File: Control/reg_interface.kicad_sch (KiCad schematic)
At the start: 16 parts, among them J5 Conn_01x04, J6 Conn_01x04, J7 Conn_01x02, J8 Conn_01x04, U10 74AHC1G08, U11 74AHC1G04, U12 74AHC1G32, U13 74AHC1G00, U14 74AHC1G32, U15 74HC173

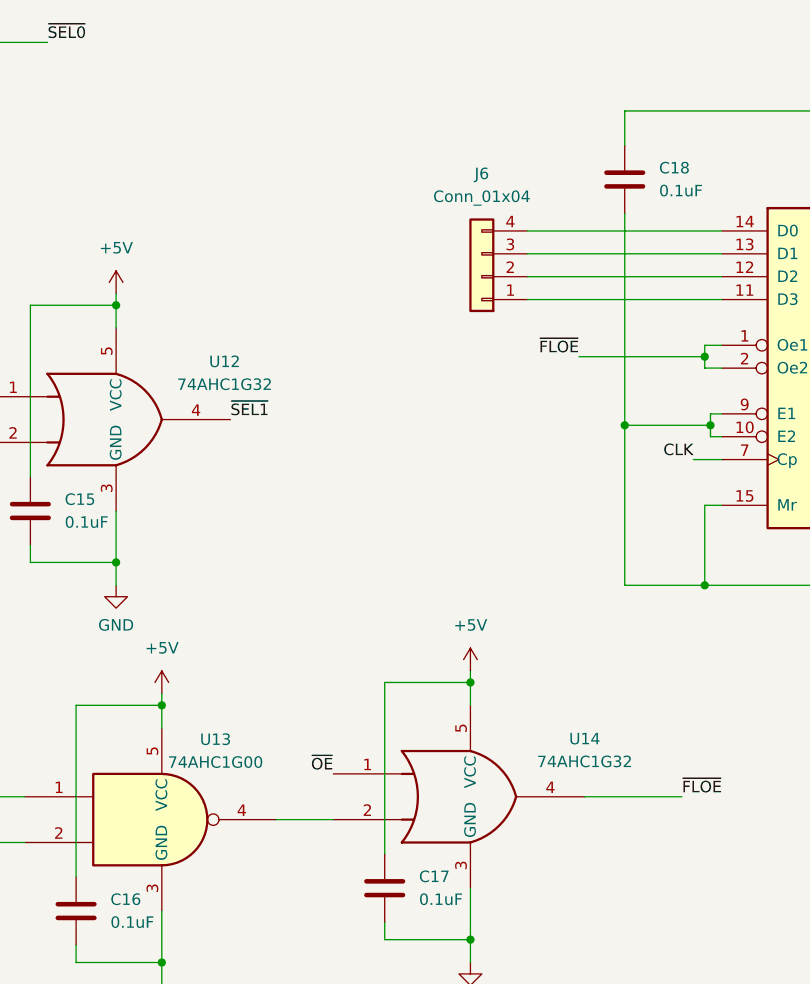
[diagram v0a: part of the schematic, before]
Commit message: Cleanup, added photos and README overhaul
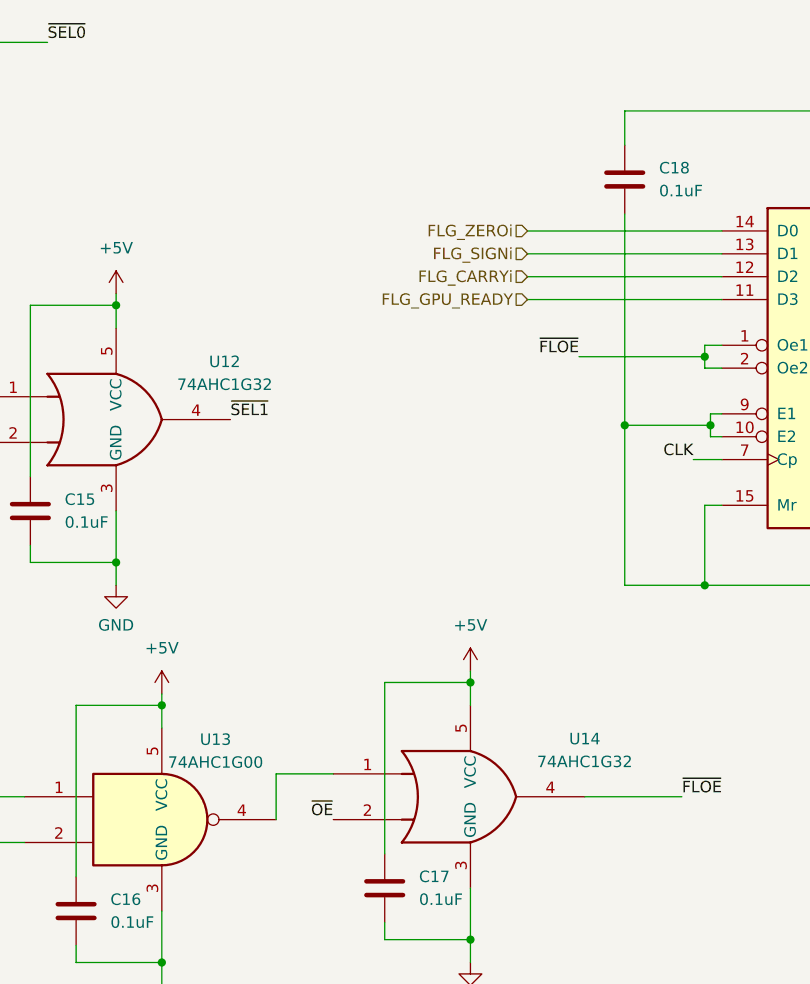
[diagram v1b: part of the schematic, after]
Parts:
- removed J6: Conn_01x04, Connector_PinSocket_2.54mm:PinSocket_1x04_P2.54mm_Vertical, symbol Connector_Generic:Conn_01x04
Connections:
- net ~{OE}: now also U14.2; no longer U14.1
- net at U13.4: now also U14.1; no longer U14.2
- net FLG_GPU_READY: now reaches U15.11 (D3)
- net FLG_CARRYi: now reaches U15.12 (D2)
- net FLG_SIGNi: now reaches U15.13 (D1)
- net FLG_ZEROi: now reaches U15.14 (D0)
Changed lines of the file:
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@@
+	(wire
+		(pts
+			(xy 111.125 109.22) (xy 111.125 104.14)
+		)
+		(stroke
+			(width 0)
+			(type default)
+		)
+	)
 	(wire
 		(pts
@@
 	(wire
 		(pts
-			(xy 111.125 109.22) (xy 117.475 109.22)
-		)
-		(stroke
-			(width 0)
-			(type default)
-		)
-	)
-	(wire
-		(pts
 			(xy 98.425 119.38) (xy 98.425 125.095)
 		)
@@
 		(pts
 			(xy 64.135 80.645) (xy 78.105 80.645)
+		)
+		(stroke
+			(width 0)
+			(type default)
+		)
+	)
+	(wire
+		(pts
+			(xy 111.125 104.14) (xy 117.475 104.14)
 		)
 		(stroke
@@
 		)
 	)
+	(label "~{OE}"
+		(at 117.475 109.22 180)
+		(effects
+			(font
+				(size 1.27 1.27)
+			)
+			(justify right bottom)
+		)
+	)
 	(label "R1"
 		(at 26.035 28.575 0)
@@
 		)
 	)
-	(label "~{OE}"
-		(at 117.475 104.14 180)
-		(effects
-			(font
-				(size 1.27 1.27)
-			)
-			(justify right bottom)
-		)
-	)
 	(label "R2"
 		(at 73.025 22.86 180)
@@
 			)
 			(justify right bottom)
+		)
+	)
+	(hierarchical_label "FLG_GPU_READY"
+		(shape input)
+		(at 139.065 51.435 180)
+		(effects
+			(font
+				(size 1.27 1.27)
+			)
+			(justify right)
+		)
+	)
+	(hierarchical_label "FLG_SIGNi"
+		(shape input)
+		(at 139.065 46.355 180)
+		(effects
+			(font
+				(size 1.27 1.27)
+			)
+			(justify right)
+		)
+	)
+	(hierarchical_label "FLG_ZEROi"
+		(shape input)
+		(at 139.065 43.815 180)
+		(effects
+			(font
+				(size 1.27 1.27)
+			)
+			(justify right)
+		)
+	)
+	(hierarchical_label "FLG_CARRYi"
+		(shape input)
+		(at 139.065 48.895 180)
+		(effects
+			(font
+				(size 1.27 1.27)
+			)
+			(justify right)
 		)
 	)
@@
 	)
 	(symbol
+		(lib_id "Device:C")
+		(at 37.465 55.88 0)
+		(unit 1)
+		(exclude_from_sim no)
+		(in_bom yes)
+		(on_board yes)
+		(dnp no)
+		(fields_autoplaced yes)
+		(property "Reference" "C13"
+			(at 40.64 54.6099 0)
+			(effects
+				(font
+					(size 1.27 1.27)
+				)
+				(justify left)
+			)
+		)
+		(property "Value" "0.1uF"
+			(at 40.64 57.1499 0)
+			(effects
+				(font
+					(size 1.27 1.27)
+				)
+				(justify left)
+			)
+		)
+		(property "Footprint" "Capacitor_SMD:C_0603_1608Metric"
+			(at 38.4302 59.69 0)
+			(effects
+				(font
+					(size 1.27 1.27)
+				)
+				(hide yes)
+			)
+		)
+		(property "Datasheet" "~"
+			(at 37.465 55.88 0)
+			(effects
+				(font
+					(size 1.27 1.27)
+				)
+				(hide yes)
+			)
+		)
+		(property "Description" "Unpolarized capacitor"
+			(at 37.465 55.88 0)
+			(effects
+				(font
+					(size 1.27 1.27)
+				)
+				(hide yes)
+			)
+		)
+		(pin "2"
+		)
+		(pin "1"
+		)
+		(instances
+			(project ""
+				(path "/0a4a6030-43dc-471b-9d34-a62eb343ab9f/7ff91962-7335-4b83-b844-8b8ab2201f13"
+					(reference "C13")
+					(unit 1)
+				)
+			)
+		)
+	)
+	(symbol
 		(lib_id "power:+5V")
 		(at 132.715 92.71 0)
@@
 				(path "/0a4a6030-43dc-471b-9d34-a62eb343ab9f/7ff91962-7335-4b83-b844-8b8ab2201f13"
 					(reference "#PWR034")
-					(unit 1)
-				)
-			)
-		)
-	)
-	(symbol
-		(lib_id "Connector_Generic:Conn_01x04")
-		(at 133.985 48.895 180)
-		(unit 1)
-		(exclude_from_sim no)
-		(in_bom yes)
-		(on_board yes)
-		(dnp no)
-		(fields_autoplaced yes)
-		(property "Reference" "J6"
-			(at 133.985 37.465 0)
-			(effects
-				(font
-					(size 1.27 1.27)
-				)
-			)
-		)
-		(property "Value" "Conn_01x04"
-			(at 133.985 40.005 0)
-			(effects
-				(font
-					(size 1.27 1.27)
-				)
-			)
-		)
-		(property "Footprint" "Connector_PinSocket_2.54mm:PinSocket_1x04_P2.54mm_Vertical"
-			(at 133.985 48.895 0)
-			(effects
-				(font
-					(size 1.27 1.27)
-				)
-				(hide yes)
-			)
-		)
-		(property "Datasheet" "~"
-			(at 133.985 48.895 0)
-			(effects
-				(font
-					(size 1.27 1.27)
-				)
-				(hide yes)
-			)
-		)
-		(property "Description" "Generic connector, single row, 01x04, script generated (kicad-library-utils/schlib/autogen/connector/)"
-			(at 133.985 48.895 0)
-			(effects
-				(font
-					(size 1.27 1.27)
-				)
-				(hide yes)
-			)
-		)
-		(pin "1"
-		)
-		(pin "4"
-		)
-		(pin "3"
-		)
-		(pin "2"
-		)
-		(instances
-			(project ""
-				(path "/0a4a6030-43dc-471b-9d34-a62eb343ab9f/7ff91962-7335-4b83-b844-8b8ab2201f13"
-					(reference "J6")
-					(unit 1)
-				)
-			)
-			(project "Memory Controller"
-				(path "/a2e955d2-87ce-495b-9d0c-0c0d88eefe1c/23deaedf-911d-40f3-b431-d452d68aefd2"
-					(reference "J8")
 					(unit 1)
 				)
@@
 					(unit 1)
 				)
-			)
-		)
-	)
-	(symbol
-		(lib_id "Device:C")
-		(at 37.465 55.88 0)
-		(unit 1)
-		(exclude_from_sim no)
-		(in_bom yes)
-		(on_board yes)
-		(dnp no)
-		(fields_autoplaced yes)
-		(property "Reference" "C13"
-			(at 40.64 54.6099 0)
-			(effects
-				(font
-					(size 1.27 1.27)
-				)
-				(justify left)
-			)
-		)
-		(property "Value" "0.1uF"
-			(at 40.64 57.1499 0)
-			(effects
-				(font
-					(size 1.27 1.27)
-				)
-				(justify left)
-			)
-		)
-		(property "Footprint" "Capacitor_SMD:C_0603_1608Metric"
-			(at 38.4302 59.69 0)
-			(effects
-				(font
-					(size 1.27 1.27)
-				)
-				(hide yes)
-			)
-		)
-		(property "Datasheet" "~"
-			(at 37.465 55.88 0)
-			(effects
-				(font
-					(size 1.27 1.27)
-				)
-				(hide yes)
-			)
-		)
-		(property "Description" "Unpolarized capacitor"
-			(at 37.465 55.88 0)
-			(effects
-				(font
-					(size 1.27 1.27)
-				)
-				(hide yes)
-			)
-		)
-		(pin "2"
-		)
-		(pin "1"
-		)
-		(instances
-			(project ""
-				(path "/0a4a6030-43dc-471b-9d34-a62eb343ab9f/7ff91962-7335-4b83-b844-8b8ab2201f13"
-					(reference "C13")
-					(unit 1)
-				)

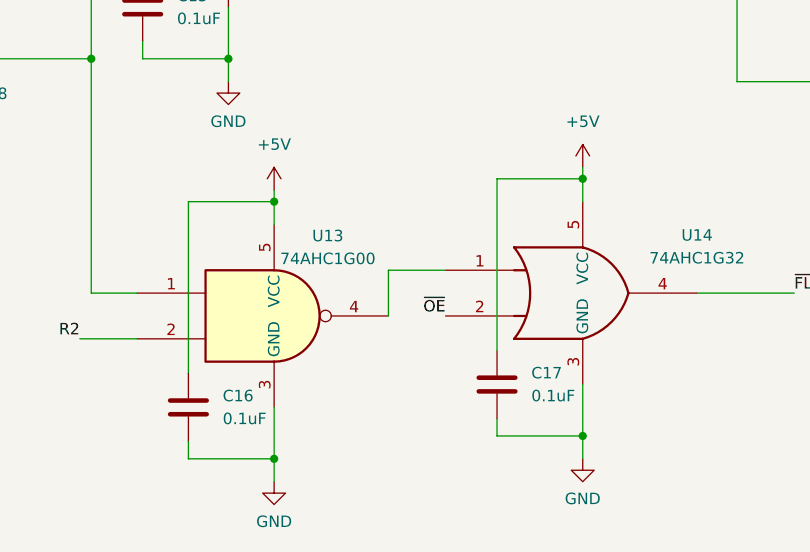
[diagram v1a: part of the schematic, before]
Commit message: Finalized Control unit for fabrication
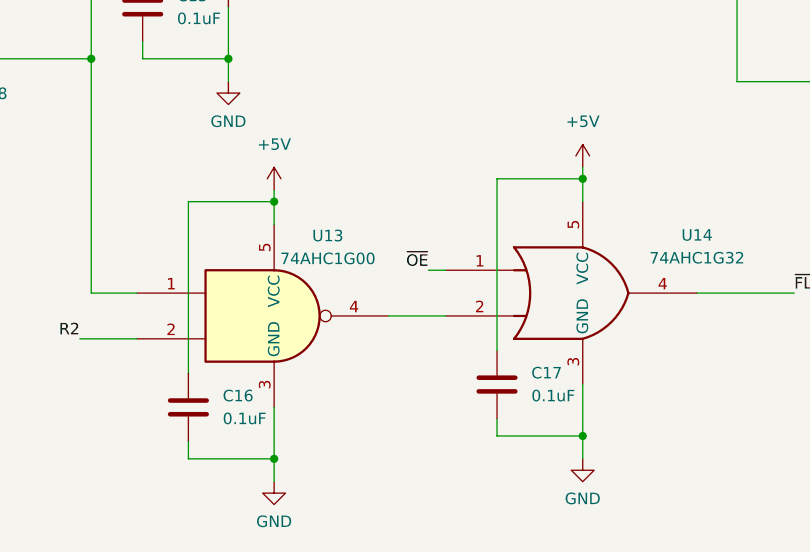
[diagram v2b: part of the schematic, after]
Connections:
- net ~{OE}: now also U14.1; no longer U14.2
- net at U13.4: now also U14.2; no longer U14.1
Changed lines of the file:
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@@
-	(wire
-		(pts
-			(xy 111.125 109.22) (xy 111.125 104.14)
-		)
-		(stroke
-			(width 0)
-			(type default)
-		)
-	)
 	(wire
 		(pts
@@
 	(wire
 		(pts
+			(xy 111.125 109.22) (xy 117.475 109.22)
+		)
+		(stroke
+			(width 0)
+			(type default)
+		)
+	)
+	(wire
+		(pts
 			(xy 41.91 94.615) (xy 41.91 96.52)
 		)
@@
 	(wire
 		(pts
+			(xy 115.57 104.14) (xy 117.475 104.14)
+		)
+		(stroke
+			(width 0)
+			(type default)
+		)
+	)
+	(wire
+		(pts
 			(xy 88.9 123.19) (xy 88.9 125.095)
 		)
@@
 	(wire
 		(pts
-			(xy 111.125 104.14) (xy 117.475 104.14)
-		)
-		(stroke
-			(width 0)
-			(type default)
-		)
-	)
-	(wire
-		(pts
 			(xy 83.82 80.645) (xy 93.345 80.645)
 		)
@@
 			(width 0)
 			(type default)
+		)
+	)
+	(label "~{OE}"
+		(at 115.57 104.14 180)
+		(effects
+			(font
+				(size 1.27 1.27)
+			)
+			(justify right bottom)
 		)
 	)
@@
 		)
 	)
-	(label "~{OE}"
-		(at 117.475 109.22 180)
-		(effects
-			(font
-				(size 1.27 1.27)
-			)
-			(justify right bottom)
-		)
-	)

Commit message: Updated control unit and finalized for fabrication
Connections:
- net FLG_CARRY: no longer names the net of J8.3 (Pin_3), U15.5 (Q2)
- net FLG_SIGN: no longer names the net of J8.2 (Pin_2), U15.4 (Q1)
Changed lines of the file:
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@@
-	)
-	(junction
-		(at 193.675 48.895)
-		(diameter 0)
-		(color 0 0 0 0)
 	)
 	(junction
@@
 	)
 	(junction
-		(at 190.5 46.355)
-		(diameter 0)
-		(color 0 0 0 0)
-	)
-	(junction
 		(at 132.715 93.98)
 		(diameter 0)
@@
 	(wire
 		(pts
-			(xy 190.5 46.355) (xy 190.5 52.705)
-		)
-		(stroke
-			(width 0)
-			(type default)
-		)
-	)
-	(wire
-		(pts
-			(xy 157.48 69.215) (xy 160.655 69.215)
-		)
-		(stroke
-			(width 0)
-			(type default)
-		)
-	)
-	(wire
-		(pts
 			(xy 88.9 96.52) (xy 98.425 96.52)
 		)
@@
 	(wire
 		(pts
-			(xy 190.5 46.355) (xy 186.055 46.355)
+			(xy 186.055 46.355) (xy 199.39 46.355)
 		)
 		(stroke
@@
 	(wire
 		(pts
-			(xy 199.39 48.895) (xy 193.675 48.895)
-		)
-		(stroke
-			(width 0)
-			(type default)
-		)
-	)
-	(wire
-		(pts
 			(xy 149.86 30.48) (xy 173.355 30.48)
 		)
@@
 	(wire
 		(pts
-			(xy 199.39 46.355) (xy 190.5 46.355)
-		)
-		(stroke
-			(width 0)
-			(type default)
-		)
-	)
-	(wire
-		(pts
 			(xy 158.75 59.055) (xy 160.655 59.055)
 		)
@@
 	(wire
 		(pts
+			(xy 146.05 69.215) (xy 160.655 69.215)
+		)
+		(stroke
+			(width 0)
+			(type default)
+		)
+	)
+	(wire
+		(pts
 			(xy 98.425 119.38) (xy 98.425 125.095)
 		)
@@
 	(wire
 		(pts
-			(xy 193.675 48.895) (xy 193.675 52.705)
-		)
-		(stroke
-			(width 0)
-			(type default)
-		)
-	)
-	(wire
-		(pts
 			(xy 51.435 90.805) (xy 51.435 96.52)
 		)
@@
 	(wire
 		(pts
-			(xy 193.675 48.895) (xy 186.055 48.895)
+			(xy 186.055 48.895) (xy 199.39 48.895)
 		)
 		(stroke
@@
 			)
 			(justify left bottom)
-		)
-	)
-	(label "CLK"
-		(at 157.48 69.215 180)
-		(effects
-			(font
-				(size 1.27 1.27)
-			)
-			(justify right bottom)
 		)
 	)
@@
 		)
 	)
-	(hierarchical_label "FLG_CARRY"
-		(shape output)
-		(at 193.675 52.705 270)
-		(effects
-			(font
-				(size 1.27 1.27)
-			)
-			(justify right)
-		)
-	)
 	(hierarchical_label "FLG_ZERO"
 		(shape output)
@@
 		)
 	)
-	(hierarchical_label "FLG_SIGN"
-		(shape output)
-		(at 190.5 52.705 270)
-		(effects
-			(font
+	(hierarchical_label "CLK"
+		(shape input)
+		(at 146.05 69.215 180)
+		(effects
+			(font
